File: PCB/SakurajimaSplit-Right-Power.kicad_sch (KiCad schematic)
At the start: 19 parts, among them J21 USB-C to Right-Half, U4 TLV76733DRVR, U6 USBLC6-2SC6

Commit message: feat(pcb): assign all footprints
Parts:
- C20: renamed from C9; footprint (none) -> Capacitor_SMD:C_0805_2012Metric
- C21: renamed from C10; footprint (none) -> Capacitor_SMD:C_0805_2012Metric
- C22: renamed from C11; footprint (none) -> Capacitor_SMD:C_0805_2012Metric
- D26: renamed from D2; footprint (none) -> Diode_SMD:D_SOD-123
- D27: renamed from D3; footprint (none) -> LED_SMD:LED_0603_1608Metric
- J39: renamed from J21; footprint (none) -> Connector_USB:USB_C_Receptacle_G-Switch_GT-USB-7010ASV
- JP3: renamed from JP1; footprint (none) -> Jumper:SolderJumper-2_P1.3mm_Open_TrianglePad1.0x1.5mm
- JP4: renamed from JP2; footprint (none) -> Jumper:SolderJumper-2_P1.3mm_Open_TrianglePad1.0x1.5mm
- JP5, JP6: footprint (none) -> Jumper:SolderJumper-2_P1.3mm_Open_TrianglePad1.0x1.5mm
- L2: renamed from L1; footprint (none) -> Inductor_SMD:L_1210_3225Metric
- R20: renamed from R11; footprint (none) -> Resistor_SMD:R_0603_1608Metric
- TP20: renamed from TP9; footprint (none) -> TestPoint:TestPoint_Pad_2.0x2.0mm
- TP21: renamed from TP10; footprint (none) -> TestPoint:TestPoint_Pad_2.0x2.0mm
- TP22: renamed from TP11; footprint (none) -> TestPoint:TestPoint_Pad_2.0x2.0mm
- TP23: renamed from TP15; footprint (none) -> TestPoint:TestPoint_Pad_2.0x2.0mm
- TP24: renamed from TP14; footprint (none) -> TestPoint:TestPoint_Pad_2.0x2.0mm
- renumbered U4 to U8, U6 to U9

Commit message: fix(sch): fix matrix diode designators not starting from 1
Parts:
- renumbered D26 to D47, D27 to D48
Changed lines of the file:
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@@
 		(dnp no)
 		(fields_autoplaced yes)
-		(property "Reference" "D26"
+		(property "Reference" "D47"
 			(at 271.4625 115.57 0)
 			(effects
@@
 			(project "SakurajimaSplit"
 				(path "/2049b6de-7453-46e1-ab60-70116abff9d6/2fb40ee0-3e4b-4e2d-8d4c-b78786a3c10e/6e8a9959-b63f-4a6d-a74b-37ddc14e864e"
-					(reference "D26")
+					(reference "D47")
 					(unit 1)
 				)
@@
 		(dnp no)
 		(fields_autoplaced yes)
-		(property "Reference" "D27"
+		(property "Reference" "D48"
 			(at 303.53 141.2874 90)
 			(effects
@@
 			(project "SakurajimaSplit"
 				(path "/2049b6de-7453-46e1-ab60-70116abff9d6/2fb40ee0-3e4b-4e2d-8d4c-b78786a3c10e/6e8a9959-b63f-4a6d-a74b-37ddc14e864e"
-					(reference "D27")
+					(reference "D48")
 					(unit 1)
 				)

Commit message: feat(sch): add spi flash, remove rotary encoder, fix footprints
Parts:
- TP20, TP21, TP22, TP23, TP24: footprint TestPoint:TestPoint_Pad_2.0x2.0mm -> Hayata_Lib:TestPoint_Pad_Circular_1.3mm
- renumbered C20 to C14, C21 to C15, C22 to C16, J39 to J31, R20 to R12
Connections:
- net VBUS: no longer TP20.1
- net at C14.1, JP3.2 (B), L2.1: now also TP20.1
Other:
- moved on the sheet: TP20
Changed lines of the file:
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@@
-	)
-	(junction
-		(at 157.48 123.19)
-		(diameter 0)
-		(color 0 0 0 0)
 	)
 	(junction
@@
 	)
 	(junction
+		(at 224.79 134.62)
+		(diameter 0)
+		(color 0 0 0 0)
+	)
+	(junction
 		(at 144.78 123.19)
 		(diameter 0)
@@
 	(wire
 		(pts
-			(xy 144.78 123.19) (xy 157.48 123.19)
+			(xy 144.78 123.19) (xy 172.72 123.19)
 		)
 		(stroke
@@
 	(wire
 		(pts
+			(xy 224.79 134.62) (xy 233.68 134.62)
+		)
+		(stroke
+			(width 0)
+			(type default)
+		)
+	)
+	(wire
+		(pts
 			(xy 257.81 134.62) (xy 261.62 134.62)
 		)
@@
 	(wire
 		(pts
-			(xy 194.31 134.62) (xy 233.68 134.62)
+			(xy 194.31 134.62) (xy 224.79 134.62)
 		)
 		(stroke
@@
 		(pts
 			(xy 233.68 134.62) (xy 240.03 134.62)
-		)
-		(stroke
-			(width 0)
-			(type default)
-		)
-	)
-	(wire
-		(pts
-			(xy 157.48 123.19) (xy 172.72 123.19)
 		)
 		(stroke
@@
 			)
 		)
-		(property "Footprint" "TestPoint:TestPoint_Pad_2.0x2.0mm"
+		(property "Footprint" "Hayata_Lib:TestPoint_Pad_Circular_1.3mm"
 			(at 262.89 134.62 0)
 			(effects
@@
 		(dnp no)
 		(fields_autoplaced yes)
-		(property "Reference" "R20"
+		(property "Reference" "R12"
 			(at 302.26 148.5899 0)
 			(effects
@@
 			(project "SakurajimaSplit"
 				(path "/2049b6de-7453-46e1-ab60-70116abff9d6/2fb40ee0-3e4b-4e2d-8d4c-b78786a3c10e/6e8a9959-b63f-4a6d-a74b-37ddc14e864e"
-					(reference "R20")
+					(reference "R12")
 					(unit 1)
 				)
@@
 		(dnp no)
 		(fields_autoplaced yes)
-		(property "Reference" "J39"
+		(property "Reference" "J31"
 			(at 118.11 115.57 0)
 			(effects
@@
 			(project "SakurajimaSplit"
 				(path "/2049b6de-7453-46e1-ab60-70116abff9d6/2fb40ee0-3e4b-4e2d-8d4c-b78786a3c10e/6e8a9959-b63f-4a6d-a74b-37ddc14e864e"
-					(reference "J39")
+					(reference "J31")
 					(unit 1)
 				)
@@
 		(dnp yes)
 		(fields_autoplaced yes)
-		(property "Reference" "C20"
+		(property "Reference" "C14"
 			(at 237.49 139.6999 0)
 			(effects
@@
 			(project "SakurajimaSplit"
 				(path "/2049b6de-7453-46e1-ab60-70116abff9d6/2fb40ee0-3e4b-4e2d-8d4c-b78786a3c10e/6e8a9959-b63f-4a6d-a74b-37ddc14e864e"
-					(reference "C20")
+					(reference "C14")
 					(unit 1)
 				)
@@
 	(symbol
 		(lib_id "Connector:TestPoint")
-		(at 157.48 123.19 0)
+		(at 224.79 134.62 0)
 		(unit 1)
 		(exclude_from_sim no)
@@
 		(dnp no)
 		(property "Reference" "TP20"
-			(at 159.258 119.634 0)
+			(at 226.568 131.064 0)
 			(effects
 				(font
@@
 		)
 		(property "Value" "VBUS"
-			(at 158.75 121.92 0)
+			(at 226.06 133.35 0)
 			(effects
 				(font
@@
 			)
 		)
-		(property "Footprint" "TestPoint:TestPoint_Pad_2.0x2.0mm"
-			(at 162.56 123.19 0)
+		(property "Footprint" "Hayata_Lib:TestPoint_Pad_Circular_1.3mm"
+			(at 229.87 134.62 0)
 			(effects
 				(font
@@
 		)
 		(property "Datasheet" "~"
-			(at 162.56 123.19 0)
+			(at 229.87 134.62 0)
 			(effects
 				(font
@@
 		)
 		(property "Description" "test point"
-			(at 157.48 123.19 0)
+			(at 224.79 134.62 0)
 			(effects
 				(font
@@
 		)
 		(property "Distributor Link" ""
-			(at 157.48 123.19 0)
+			(at 224.79 134.62 0)
 			(effects
 				(font
@@
 		)
 		(property "Manufacturer" ""
-			(at 157.48 123.19 0)
+			(at 224.79 134.62 0)
 			(effects
 				(font
@@
 		)
 		(property "Manufacturer Part No." ""
-			(at 157.48 123.19 0)
+			(at 224.79 134.62 0)
 			(effects
 				(font
@@
 		)
 		(property "Notes" ""
-			(at 157.48 123.19 0)
+			(at 224.79 134.62 0)
 			(effects
 				(font
@@
 			)
 		)
-		(property "Footprint" "TestPoint:TestPoint_Pad_2.0x2.0mm"
+		(property "Footprint" "Hayata_Lib:TestPoint_Pad_Circular_1.3mm"
 			(at 292.1 134.62 0)
 			(effects
@@
 		(dnp no)
 		(fields_autoplaced yes)
-		(property "Reference" "C21"
+		(property "Reference" "C15"
 			(at 257.81 139.6999 0)
 			(effects
@@
 			(project "SakurajimaSplit"
 				(path "/2049b6de-7453-46e1-ab60-70116abff9d6/2fb40ee0-3e4b-4e2d-8d4c-b78786a3c10e/6e8a9959-b63f-4a6d-a74b-37ddc14e864e"
-					(reference "C21")
+					(reference "C15")
 					(unit 1)
 				)
@@
 			)
 		)
-		(property "Footprint" "TestPoint:TestPoint_Pad_2.0x2.0mm"
+		(property "Footprint" "Hayata_Lib:TestPoint_Pad_Circular_1.3mm"
 			(at 161.29 138.43 0)
 			(effects
@@
 		(dnp no)
 		(fields_autoplaced yes)
-		(property "Reference" "C22"
+		(property "Reference" "C16"
 			(at 290.83 139.6999 0)
 			(effects
@@
 			(project "SakurajimaSplit"
 				(path "/2049b6de-7453-46e1-ab60-70116abff9d6/2fb40ee0-3e4b-4e2d-8d4c-b78786a3c10e/6e8a9959-b63f-4a6d-a74b-37ddc14e864e"
-					(reference "C22")
+					(reference "C16")
 					(unit 1)
 				)
@@
 			)
 		)
-		(property "Footprint" "TestPoint:TestPoint_Pad_2.0x2.0mm"
+		(property "Footprint" "Hayata_Lib:TestPoint_Pad_Circular_1.3mm"
 			(at 161.29 140.97 0)
 			(effects

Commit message: fix(sch): swap LEDs with their series resistors
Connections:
- net GND: now also D48.1 (K); no longer R12.2
- net at R12.1: now also C16.1, D47.2 (A), JP4.1 (A), TP22.1, U8.1 (OUT), U8.2 (SNS); no longer D48.1 (K)
- new net: D48.2 (A), R12.2
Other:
- moved on the sheet: D48, R12
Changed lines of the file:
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@@
 	)
 	(junction
+		(at 299.72 134.62)
+		(diameter 0)
+		(color 0 0 0 0)
+	)
+	(junction
 		(at 118.11 163.83)
 		(diameter 0)
@@
 	)
 	(junction
-		(at 299.72 134.62)
-		(diameter 0)
-		(color 0 0 0 0)
-	)
-	(junction
 		(at 287.02 134.62)
 		(diameter 0)
@@
 	(wire
 		(pts
-			(xy 250.19 134.62) (xy 254 134.62)
+			(xy 299.72 142.24) (xy 299.72 144.78)
 		)
 		(stroke
@@
 	(wire
 		(pts
-			(xy 135.89 143.51) (xy 133.35 143.51)
+			(xy 299.72 134.62) (xy 320.04 134.62)
 		)
 		(stroke
@@
 	(wire
 		(pts
-			(xy 287.02 134.62) (xy 299.72 134.62)
+			(xy 250.19 134.62) (xy 254 134.62)
 		)
 		(stroke
@@
 	(wire
 		(pts
-			(xy 118.11 166.37) (xy 118.11 163.83)
+			(xy 135.89 143.51) (xy 133.35 143.51)
 		)
 		(stroke
@@
 	(wire
 		(pts
-			(xy 110.49 161.29) (xy 110.49 163.83)
+			(xy 118.11 166.37) (xy 118.11 163.83)
 		)
 		(stroke
@@
 	(wire
 		(pts
-			(xy 299.72 134.62) (xy 299.72 137.16)
+			(xy 110.49 161.29) (xy 110.49 163.83)
 		)
 		(stroke
@@
 	(wire
 		(pts
-			(xy 299.72 144.78) (xy 299.72 147.32)
-		)
-		(stroke
-			(width 0)
-			(type default)
-		)
-	)
-	(wire
-		(pts
 			(xy 172.72 134.62) (xy 186.69 134.62)
 		)
@@
 	(wire
 		(pts
+			(xy 299.72 152.4) (xy 299.72 154.94)
+		)
+		(stroke
+			(width 0)
+			(type default)
+		)
+	)
+	(wire
+		(pts
 			(xy 257.81 134.62) (xy 261.62 134.62)
 		)
@@
 	(wire
 		(pts
+			(xy 299.72 134.62) (xy 299.72 137.16)
+		)
+		(stroke
+			(width 0)
+			(type default)
+		)
+	)
+	(wire
+		(pts
 			(xy 194.31 134.62) (xy 224.79 134.62)
 		)
@@
 	(wire
 		(pts
-			(xy 299.72 152.4) (xy 299.72 154.94)
-		)
-		(stroke
-			(width 0)
-			(type default)
-		)
-	)
-	(wire
-		(pts
 			(xy 275.59 121.92) (xy 281.94 121.92)
 		)
@@
 	(wire
 		(pts
-			(xy 299.72 134.62) (xy 320.04 134.62)
+			(xy 287.02 134.62) (xy 299.72 134.62)
 		)
 		(stroke
@@
 	(symbol
 		(lib_id "Device:R_Small")
-		(at 299.72 149.86 0)
+		(at 299.72 139.7 0)
 		(unit 1)
 		(exclude_from_sim no)
@@
 		(fields_autoplaced yes)
 		(property "Reference" "R12"
-			(at 302.26 148.5899 0)
+			(at 302.26 138.4299 0)
 			(effects
 				(font
@@
 		)
 		(property "Value" "330R"
-			(at 302.26 151.1299 0)
+			(at 302.26 140.9699 0)
 			(effects
 				(font
@@
 		)
 		(property "Footprint" "Resistor_SMD:R_0603_1608Metric"
-			(at 299.72 149.86 0)
+			(at 299.72 139.7 0)
 			(effects
 				(font
@@
 		)
 		(property "Datasheet" "~"
-			(at 299.72 149.86 0)
+			(at 299.72 139.7 0)
 			(effects
 				(font
@@
 		)
 		(property "Description" "Resistor, small symbol"
-			(at 299.72 149.86 0)
+			(at 299.72 139.7 0)
 			(effects
 				(font
@@
 		)
 		(property "Distributor Link" "https://lionelectronic.ir/products/1182-SER0603F330R"
-			(at 299.72 149.86 0)
+			(at 299.72 139.7 0)
 			(effects
 				(font
@@
 		)
 		(property "Manufacturer" "VO Sub Brand (ER)"
-			(at 299.72 149.86 0)
+			(at 299.72 139.7 0)
 			(effects
 				(font
@@
 		)
 		(property "Manufacturer Part No." "SER0603F330R"
-			(at 299.72 149.86 0)
+			(at 299.72 139.7 0)
 			(effects
 				(font
@@
 		)
 		(property "Notes" ""
-			(at 299.72 149.86 0)
+			(at 299.72 139.7 0)
 			(effects
 				(font
@@
 	(symbol
 		(lib_id "Device:LED")
-		(at 299.72 140.97 90)
+		(at 299.72 148.59 90)
 		(unit 1)
 		(exclude_from_sim no)
@@
 		(fields_autoplaced yes)
 		(property "Reference" "D48"
-			(at 303.53 141.2874 90)
+			(at 303.53 148.9074 90)
 			(effects
 				(font
@@
 		)
 		(property "Value" "PWR ind."
-			(at 303.53 143.8274 90)
+			(at 303.53 151.4474 90)
 			(effects
 				(font
@@
 		)
 		(property "Footprint" "LED_SMD:LED_0603_1608Metric"
-			(at 299.72 140.97 0)
+			(at 299.72 148.59 0)
 			(effects
 				(font
@@
 		)
 		(property "Datasheet" "~"
-			(at 299.72 140.97 0)
+			(at 299.72 148.59 0)
 			(effects
 				(font
@@
 		)
 		(property "Description" "Light emitting diode"
-			(at 299.72 140.97 0)
+			(at 299.72 148.59 0)
 			(effects
 				(font
@@
 		)
 		(property "Sim.Pins" "1=K 2=A"
-			(at 299.72 140.97 0)
+			(at 299.72 148.59 0)
 			(effects
 				(font
@@
 		)
 		(property "Distributor Link" "https://lionelectronic.ir/products/2212-XL-1608UGC-04"
-			(at 299.72 140.97 0)
+			(at 299.72 148.59 0)
 			(effects
 				(font
@@
 		)
 		(property "Manufacturer" "XINGLIGHT"
-			(at 299.72 140.97 0)
+			(at 299.72 148.59 0)
 			(effects
 				(font
@@
 		)
 		(property "Manufacturer Part No." "XL-1608UGC-04"
-			(at 299.72 140.97 0)
+			(at 299.72 148.59 0)
 			(effects
 				(font
@@
 		)
 		(property "Notes" ""
-			(at 299.72 140.97 0)
+			(at 299.72 148.59 0)
 			(effects
 				(font

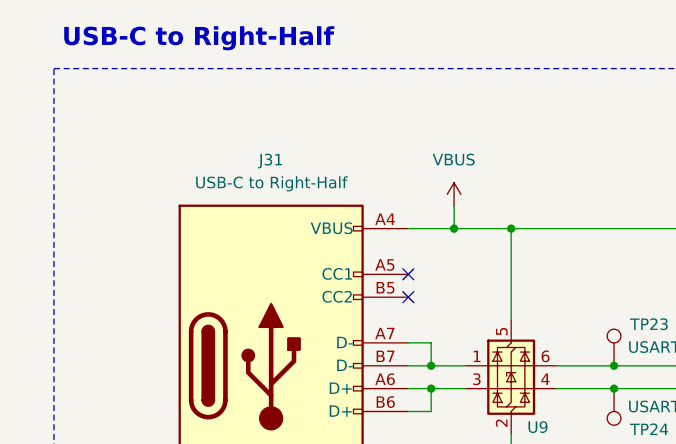
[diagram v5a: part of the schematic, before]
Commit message: feat(pcb): finish designing rough layout and update schematic
- Removed unused MCU pads
- Removed some GND testpoints
- Updated MCU connections based on PCB layout and MCU orientation
- Updated key matrix layout for a less aggressive one which feels more
  comfortable and more visually pleasing
- Re-annotated schematic
- Finished rough component placement
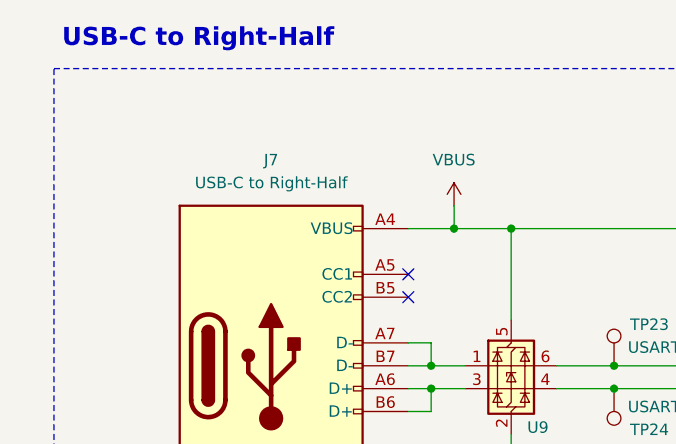
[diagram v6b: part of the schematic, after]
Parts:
- renumbered J31 to J7
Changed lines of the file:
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@@
 		(dnp no)
 		(fields_autoplaced yes)
-		(property "Reference" "#PWR051"
+		(property "Reference" "#PWR047"
 			(at 138.43 124.46 0)
 			(effects
@@
 			(project "SakurajimaSplit"
 				(path "/2049b6de-7453-46e1-ab60-70116abff9d6/2fb40ee0-3e4b-4e2d-8d4c-b78786a3c10e/6e8a9959-b63f-4a6d-a74b-37ddc14e864e"
-					(reference "#PWR051")
+					(reference "#PWR047")
 					(unit 1)
 				)
@@
 		(dnp no)
 		(fields_autoplaced yes)
-		(property "Reference" "#PWR055"
+		(property "Reference" "#PWR051"
 			(at 254 153.67 0)
 			(effects
@@
 			(project "SakurajimaSplit"
 				(path "/2049b6de-7453-46e1-ab60-70116abff9d6/2fb40ee0-3e4b-4e2d-8d4c-b78786a3c10e/6e8a9959-b63f-4a6d-a74b-37ddc14e864e"
-					(reference "#PWR055")
+					(reference "#PWR051")
 					(unit 1)
 				)
@@
 		(dnp no)
 		(fields_autoplaced yes)
-		(property "Reference" "#PWR060"
+		(property "Reference" "#PWR056"
 			(at 118.11 172.72 0)
 			(effects
@@
 			(project "SakurajimaSplit"
 				(path "/2049b6de-7453-46e1-ab60-70116abff9d6/2fb40ee0-3e4b-4e2d-8d4c-b78786a3c10e/6e8a9959-b63f-4a6d-a74b-37ddc14e864e"
-					(reference "#PWR060")
+					(reference "#PWR056")
 					(unit 1)
 				)
@@
 		(dnp no)
 		(fields_autoplaced yes)
-		(property "Reference" "#PWR053"
+		(property "Reference" "#PWR049"
 			(at 335.28 135.89 0)
 			(effects
@@
 			(project "SakurajimaSplit"
 				(path "/2049b6de-7453-46e1-ab60-70116abff9d6/2fb40ee0-3e4b-4e2d-8d4c-b78786a3c10e/6e8a9959-b63f-4a6d-a74b-37ddc14e864e"
-					(reference "#PWR053")
+					(reference "#PWR049")
 					(unit 1)
 				)
@@
 		(dnp no)
 		(fields_autoplaced yes)
-		(property "Reference" "J31"
+		(property "Reference" "J7"
 			(at 118.11 115.57 0)
 			(effects
@@
 			(project "SakurajimaSplit"
 				(path "/2049b6de-7453-46e1-ab60-70116abff9d6/2fb40ee0-3e4b-4e2d-8d4c-b78786a3c10e/6e8a9959-b63f-4a6d-a74b-37ddc14e864e"
-					(reference "J31")
+					(reference "J7")
 					(unit 1)
 				)
@@
 		(dnp no)
 		(fields_autoplaced yes)
-		(property "Reference" "#PWR057"
+		(property "Reference" "#PWR053"
 			(at 144.78 154.94 0)
 			(effects
@@
 			(project "SakurajimaSplit"
 				(path "/2049b6de-7453-46e1-ab60-70116abff9d6/2fb40ee0-3e4b-4e2d-8d4c-b78786a3c10e/6e8a9959-b63f-4a6d-a74b-37ddc14e864e"
-					(reference "#PWR057")
+					(reference "#PWR053")
 					(unit 1)
 				)
@@
 		(dnp no)
 		(fields_autoplaced yes)
-		(property "Reference" "#PWR056"
+		(property "Reference" "#PWR052"
 			(at 287.02 153.67 0)
 			(effects
@@
 			(project "SakurajimaSplit"
 				(path "/2049b6de-7453-46e1-ab60-70116abff9d6/2fb40ee0-3e4b-4e2d-8d4c-b78786a3c10e/6e8a9959-b63f-4a6d-a74b-37ddc14e864e"
-					(reference "#PWR056")
+					(reference "#PWR052")
 					(unit 1)
 				)
@@
 		(dnp no)
 		(fields_autoplaced yes)
-		(property "Reference" "#PWR054"
+		(property "Reference" "#PWR050"
 			(at 233.68 153.67 0)
 			(effects
@@
 			(project "SakurajimaSplit"
 				(path "/2049b6de-7453-46e1-ab60-70116abff9d6/2fb40ee0-3e4b-4e2d-8d4c-b78786a3c10e/6e8a9959-b63f-4a6d-a74b-37ddc14e864e"
-					(reference "#PWR054")
+					(reference "#PWR050")
 					(unit 1)
 				)
@@
 		(dnp no)
 		(fields_autoplaced yes)
-		(property "Reference" "#PWR058"
+		(property "Reference" "#PWR054"
 			(at 271.78 156.21 0)
 			(effects
@@
 			(project "SakurajimaSplit"
 				(path "/2049b6de-7453-46e1-ab60-70116abff9d6/2fb40ee0-3e4b-4e2d-8d4c-b78786a3c10e/6e8a9959-b63f-4a6d-a74b-37ddc14e864e"
-					(reference "#PWR058")
+					(reference "#PWR054")
 					(unit 1)
 				)
@@
 		(dnp no)
 		(fields_autoplaced yes)
-		(property "Reference" "#PWR052"
+		(property "Reference" "#PWR048"
 			(at 250.19 135.89 0)
 			(effects
@@
 			(project "SakurajimaSplit"
 				(path "/2049b6de-7453-46e1-ab60-70116abff9d6/2fb40ee0-3e4b-4e2d-8d4c-b78786a3c10e/6e8a9959-b63f-4a6d-a74b-37ddc14e864e"
-					(reference "#PWR052")
+					(reference "#PWR048")
 					(unit 1)
 				)
@@
 		(dnp no)
 		(fields_autoplaced yes)
-		(property "Reference" "#PWR059"
+		(property "Reference" "#PWR055"
 			(at 299.72 161.29 0)
 			(effects
@@
 			(project "SakurajimaSplit"
 				(path "/2049b6de-7453-46e1-ab60-70116abff9d6/2fb40ee0-3e4b-4e2d-8d4c-b78786a3c10e/6e8a9959-b63f-4a6d-a74b-37ddc14e864e"
-					(reference "#PWR059")
-					(unit 1)
-				)
+					(reference "#PWR055")
+					(unit 1)
+				)
